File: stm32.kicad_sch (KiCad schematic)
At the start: 36 parts, among them IC1 ADBMS6821CCSZ, J5 Conn_02x03_Top_Bottom, SW1 SW_Nidec_CAS-120A1, SW3 SW_Nidec_CAS-120A1, T1 74941301, U15 SN65HVD234, U3 STM32G474CETx, U4 SN65HVD234, U5 ADS1113IDGS, Y2 16 MHz

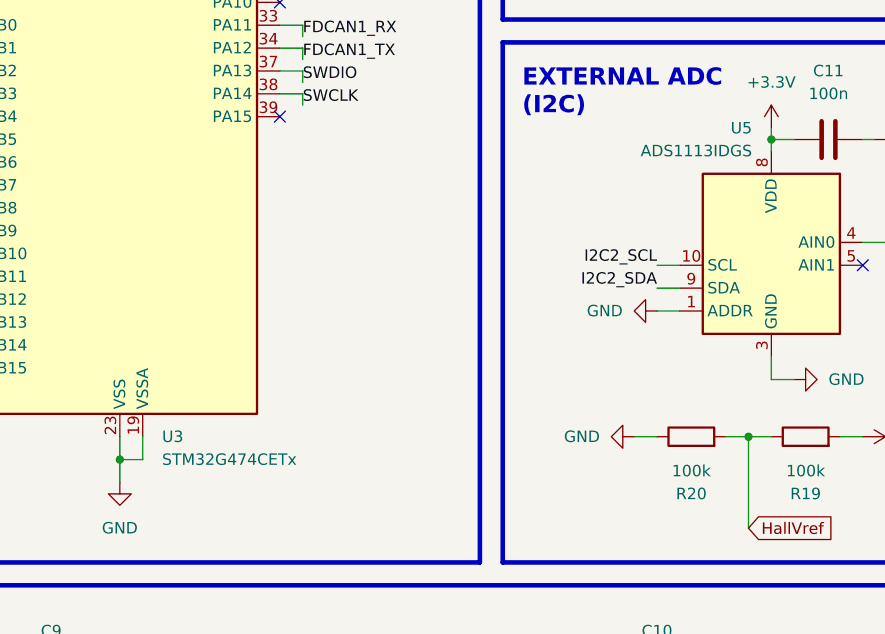
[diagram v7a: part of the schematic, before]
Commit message: Revisió dels valors de filtres, divisors de tensió i resistències
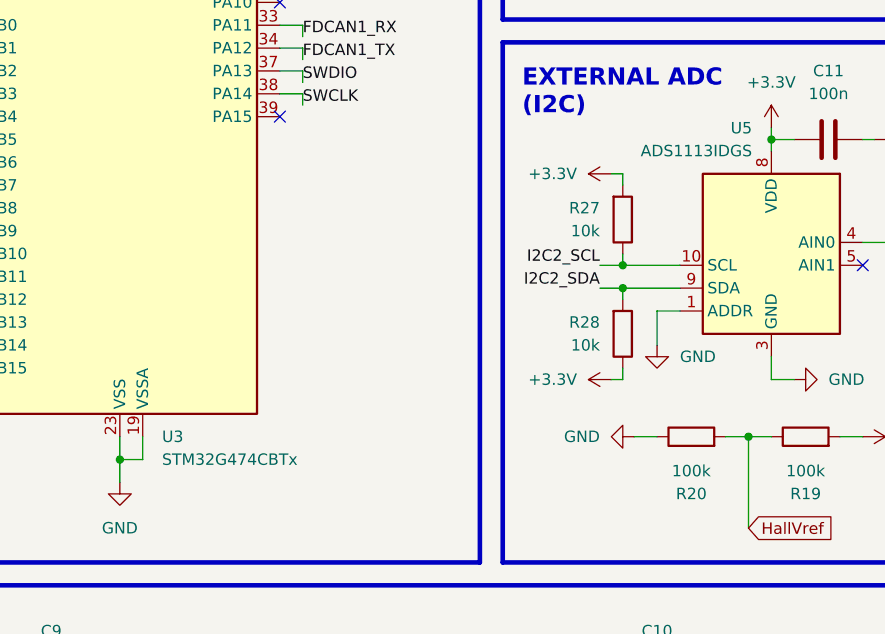
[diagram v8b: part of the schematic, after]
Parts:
- added R27, R28: 10k, Resistor_SMD:R_0201_0603Metric_Pad0.64x0.40mm_HandSolder, symbol Device:R
- U3: value STM32G474CETx -> STM32G474CBTx
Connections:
- net +3.3V: now also R27.2, R28.1
- net I2C2_SCL: now also R27.1
- net I2C2_SDA: now also R28.2
